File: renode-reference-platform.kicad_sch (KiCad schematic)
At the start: 4 parts

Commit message: [#95398] Cleanup
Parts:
- added H1, H2, H3, H4: Spacer_Drill3.7mm_H5mm_9774050151R, antmicro-footprints:Spacer_Drill3.7mm_H5mm_9774050151R, symbol antmicroMechanicalParts:Spacer_Drill3.7mm_H5mm_9774050151R
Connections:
- new net GND: H1.1, H2.1, H3.1, H4.1
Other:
- sheet IMU renamed Sensors
- sheet RPI Connector renamed Expansion Connector
- removed sheet PMOD
- sheet Expansion Connector: file rpi-expansion.kicad_sch -> expansion.kicad_sch
- sheet Expansion Connector ports: added none; removed EN_RPI_CONN, GPIO[0..27], I2C_RPI{I2C}, SPI_RPI{SPI}, UART_RPI{UART}
- sheet IOs ports: added POT1_Analog, POT2_Analog; removed none
- sheet MCU ports: added none; removed EN_PMOD, EN_RPI_CONN, GPIO[0..27], I2C3{I2C}, I2C4{I2C}, PMOD1_IO[5..8], PMOD2_IO[5..6], SPI_1{SPI}, SPI_2{SPI}, UART1{UART}, UART_3{UART}
- sheet Sensors: file imu.kicad_sch -> sensors.kicad_sch
- sheet Sensors ports: added I2C_SENSOR{I2C}; removed I2C_IMU{I2C}

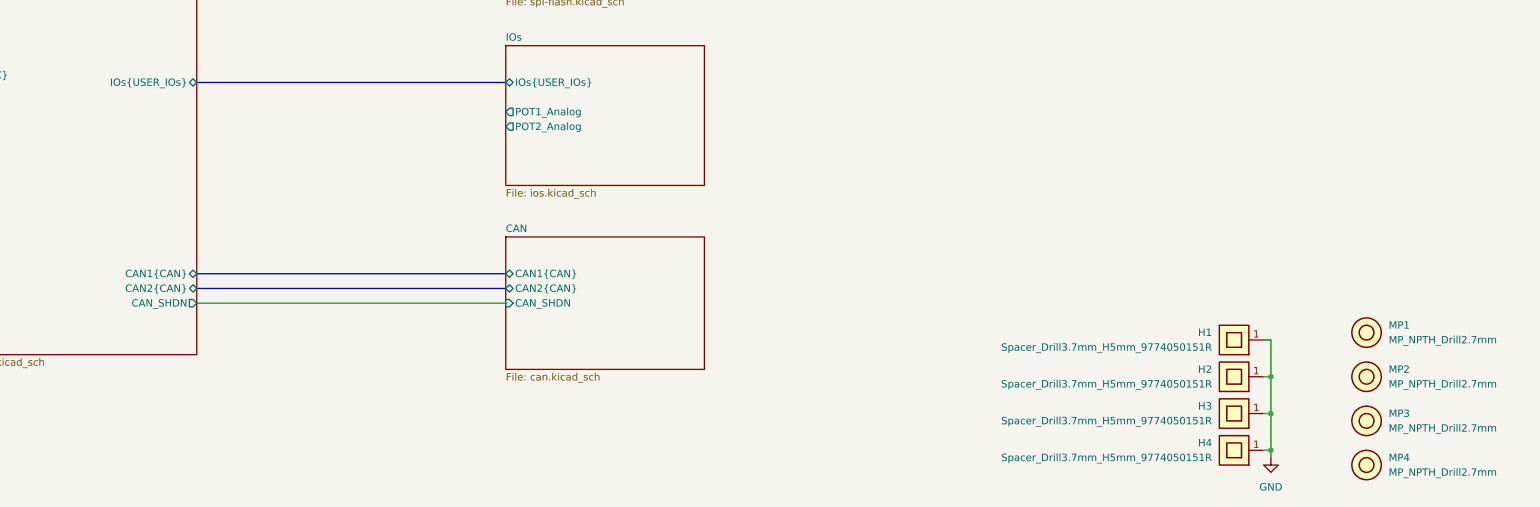
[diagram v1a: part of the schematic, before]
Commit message: [#95398] Connect potentiometers
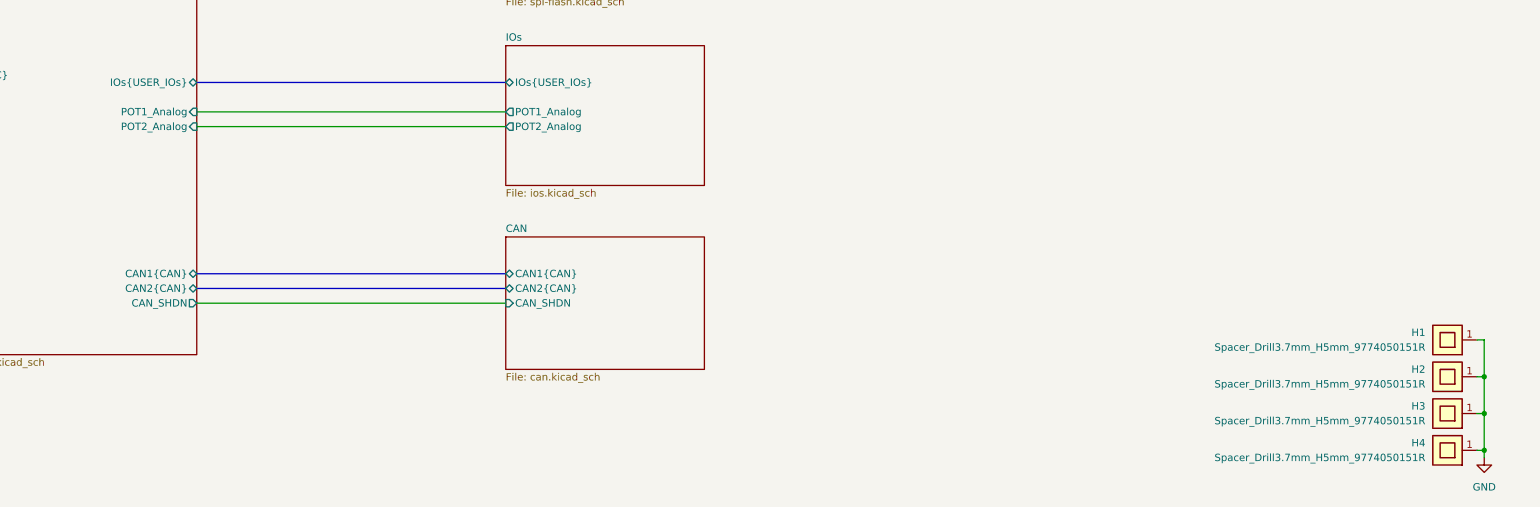
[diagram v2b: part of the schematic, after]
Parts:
- removed MP1, MP2, MP3, MP4: MP_NPTH_Drill2.7mm, antmicro-footprints:MP_NPTH_Drill2.7mm, symbol antmicroMechanicalParts:MP_NPTH_Drill2.7mm
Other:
- sheet MCU ports: added POT1_Analog, POT2_Analog; removed none
- moved on the sheet: H1, H2, H3, H4

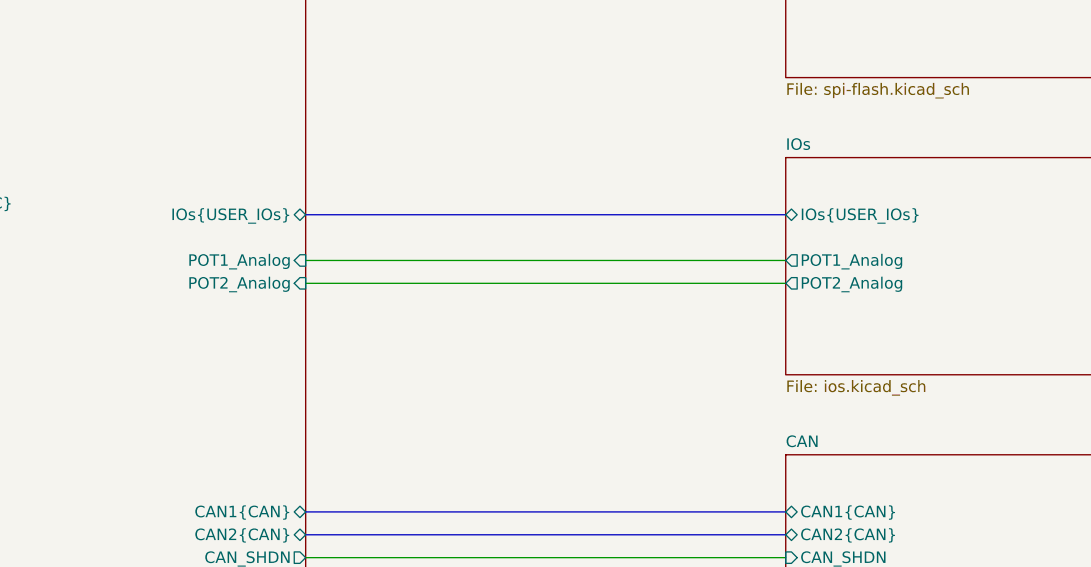
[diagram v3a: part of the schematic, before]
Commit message: [#95398] Mock main components, add BGA MCU
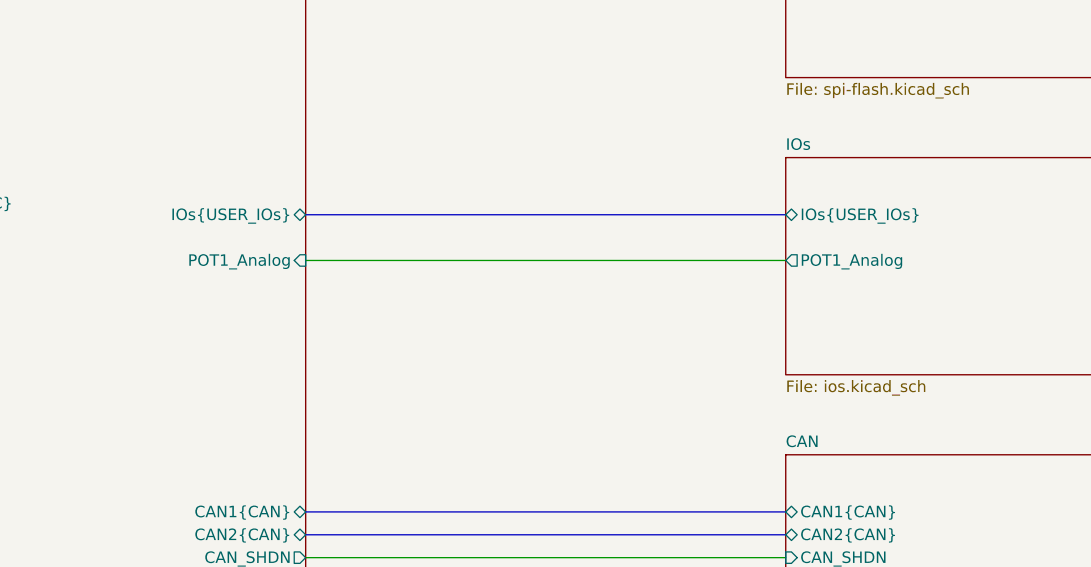
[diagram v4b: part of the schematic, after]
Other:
- sheet IOs ports: added none; removed POT2_Analog
- sheet MCU ports: added none; removed POT2_Analog
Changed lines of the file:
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@@
-	(wire
-		(pts
-			(xy 228.6 185.42) (xy 281.94 185.42)
-		)
-		(stroke
-			(width 0)
-			(type default)
-		)
-	)
 	(wire
 		(pts
@@
 			)
 		)
-		(pin "POT2_Analog" output
-			(at 281.94 185.42 180)
-			(effects
-				(font
-					(size 1.27 1.27)
-				)
-				(justify left)
-			)
-		)
 		(instances
 			(project "renode-reference-platform"
@@
 			(effects
 				(font
-					(size 1.27 1.27)
-				)
-				(justify right)
-			)
-		)
-		(pin "POT2_Analog" input
-			(at 228.6 185.42 0)
-			(effects
-				(font

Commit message: [#95398] Add markings for ETH strap resistors
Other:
- title: renode-reference-platform -> STM32H7 Renode Reference Platform
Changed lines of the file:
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@@
 	(paper "A3")
 	(title_block
-		(title "renode-reference-platform")
+		(title "STM32H7 Renode Reference Platform")
 		(date "07.04.2026")
 		(rev "1.0.0")

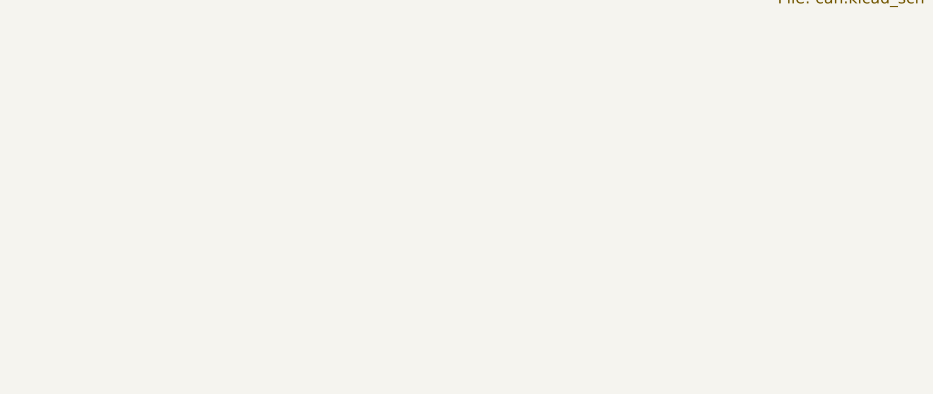
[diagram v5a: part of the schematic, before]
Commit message: [#95451] Fiducial and TP placement
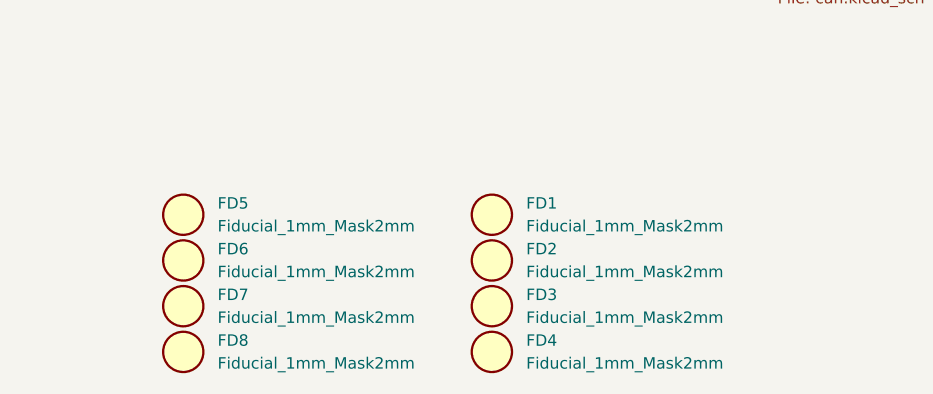
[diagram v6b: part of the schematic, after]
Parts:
- added FD1, FD2, FD3, FD4, FD5, FD6, FD7, FD8: Fiducial_1mm_Mask2mm, antmicro-footprints:Fiducial_1mm_Mask2mm, symbol antmicroFiducialMarks:Fiducial_1mm_Mask2mm

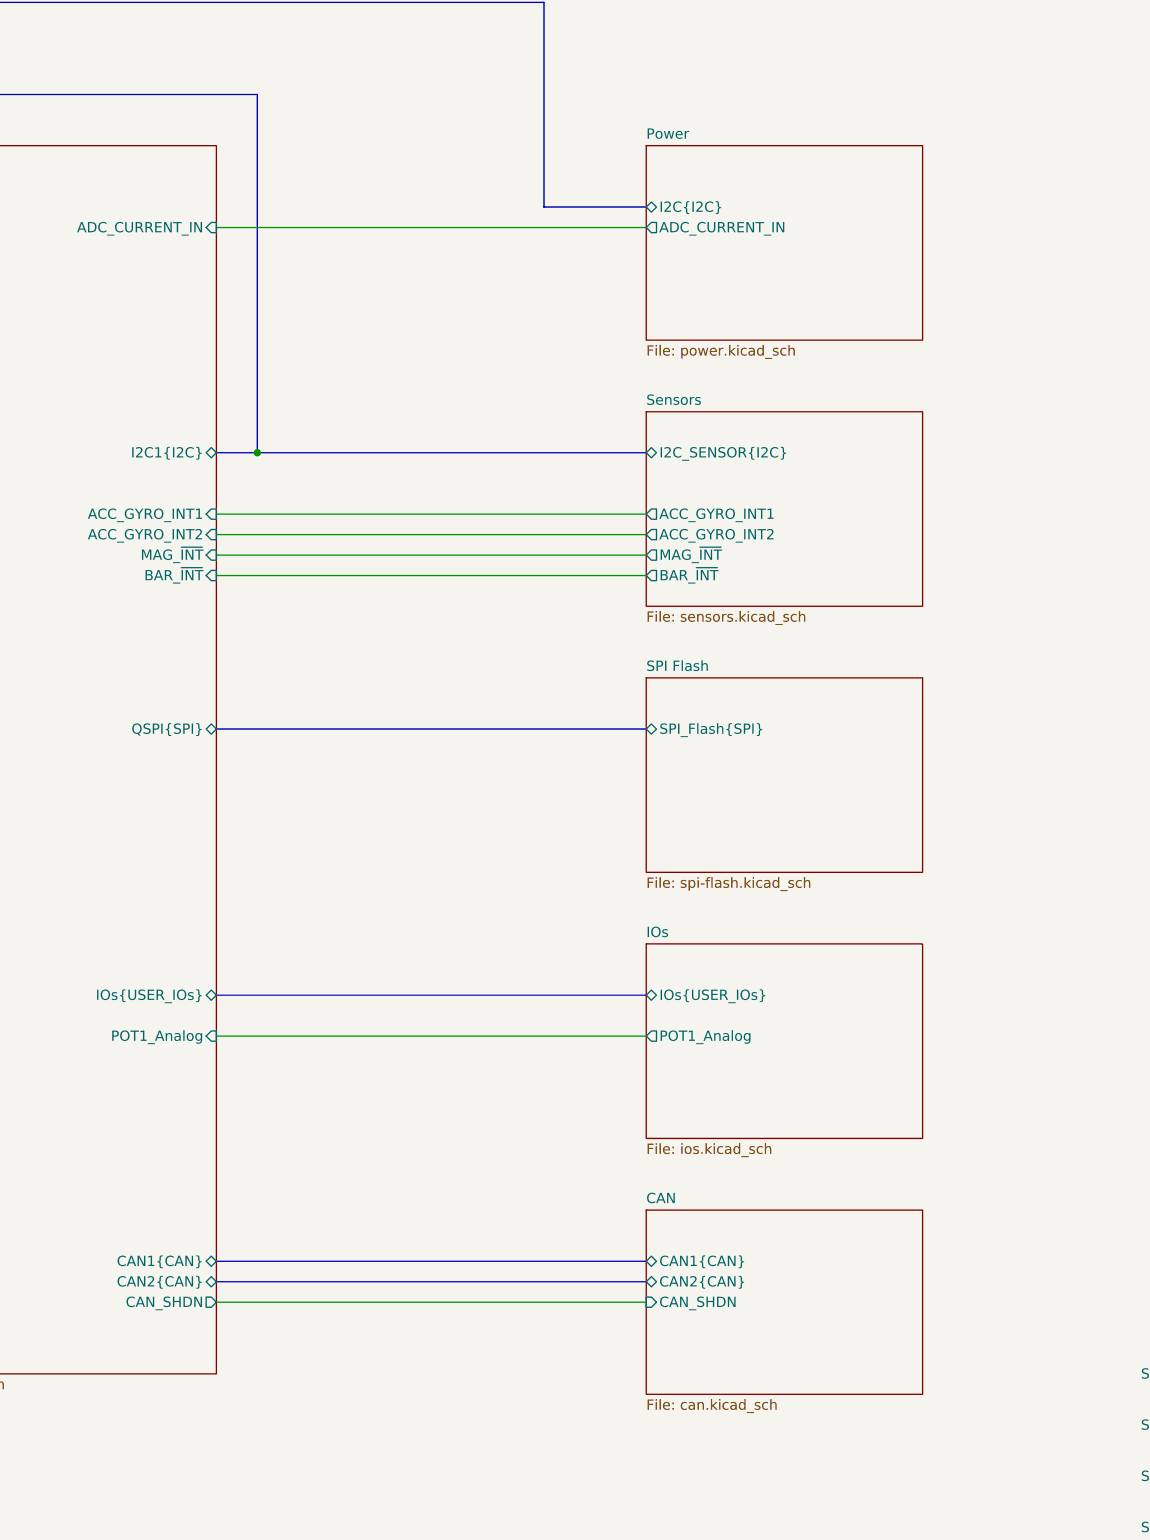
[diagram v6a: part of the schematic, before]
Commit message: [#95451] Improve placement. Add JTAG TC and ID EEPROM.
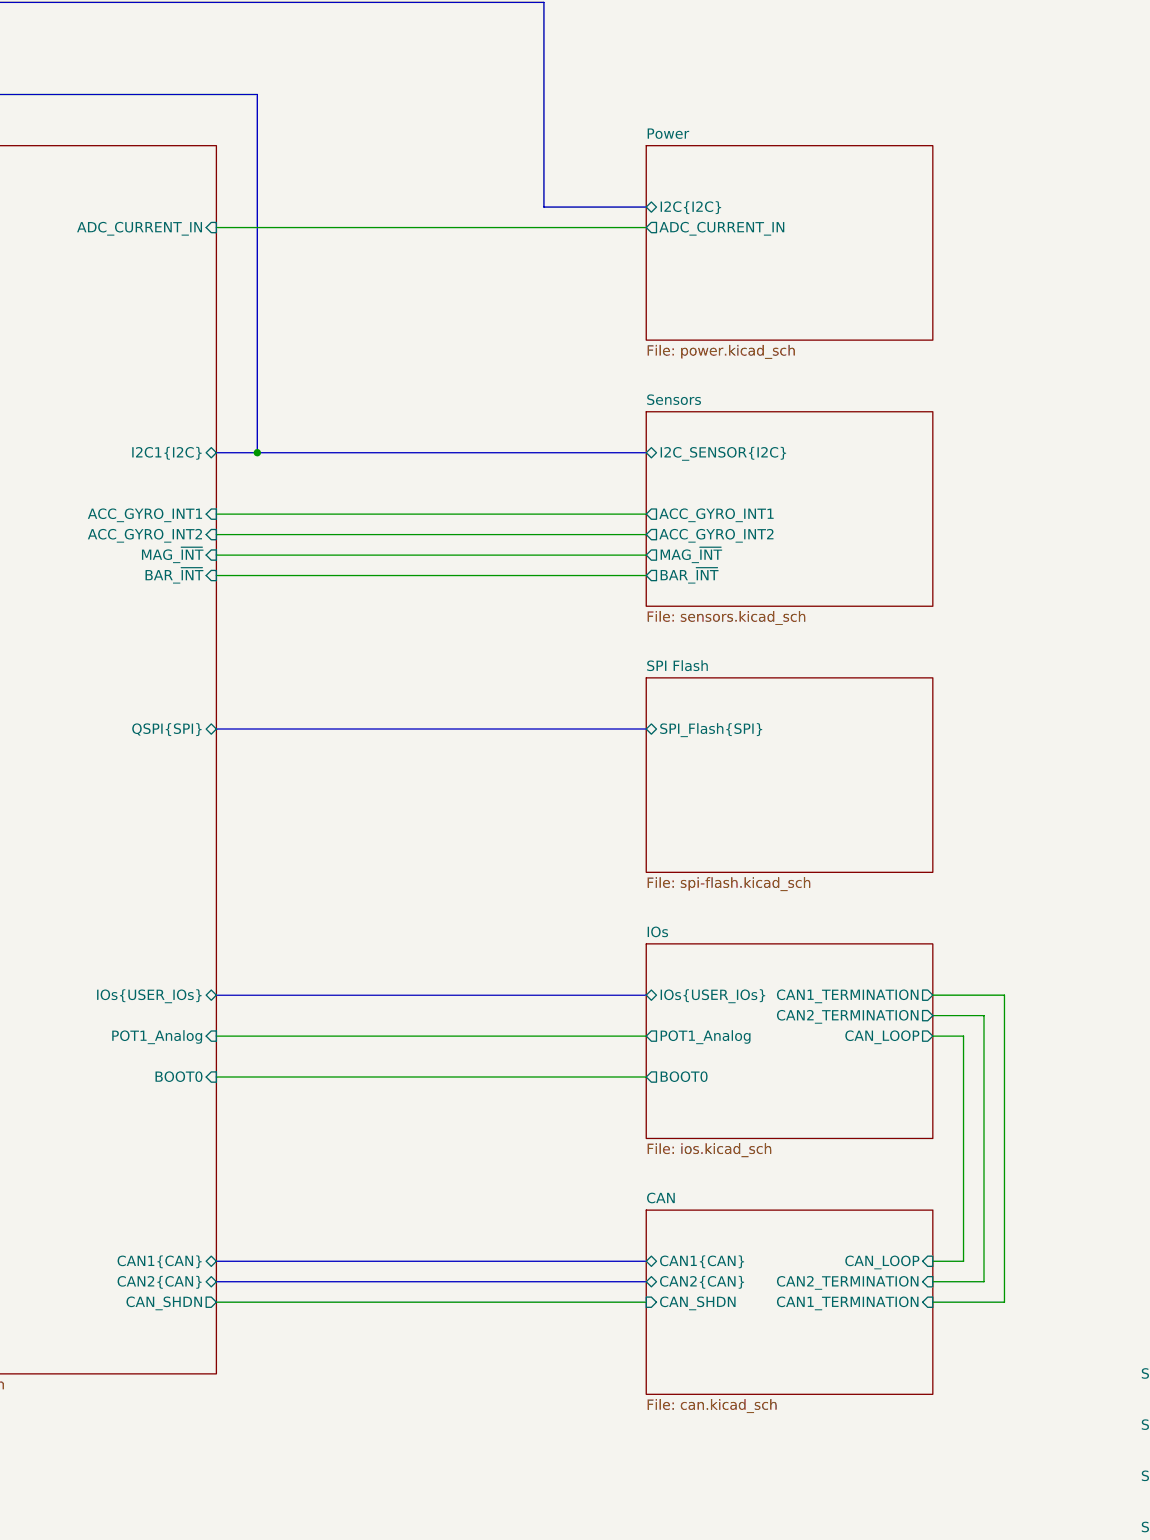
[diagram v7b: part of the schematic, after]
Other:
- sheet CAN ports: added CAN1_TERMINATION, CAN2_TERMINATION, CAN_LOOP; removed none
- sheet IOs ports: added BOOT0, CAN1_TERMINATION, CAN2_TERMINATION, CAN_LOOP; removed none
- sheet MCU ports: added BOOT0; removed none
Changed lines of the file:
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@@
+		)
+	)
+	(wire
+		(pts
+			(xy 317.5 180.34) (xy 323.85 180.34)
+		)
+		(stroke
+			(width 0)
+			(type default)
 		)
 	)
@@
 	(wire
 		(pts
+			(xy 321.31 210.82) (xy 317.5 210.82)
+		)
+		(stroke
+			(width 0)
+			(type default)
+		)
+	)
+	(wire
+		(pts
+			(xy 326.39 215.9) (xy 317.5 215.9)
+		)
+		(stroke
+			(width 0)
+			(type default)
+		)
+	)
+	(wire
+		(pts
 			(xy 228.6 82.55) (xy 281.94 82.55)
 		)
@@
 		)
 	)
+	(wire
+		(pts
+			(xy 321.31 182.88) (xy 321.31 210.82)
+		)
+		(stroke
+			(width 0)
+			(type default)
+		)
+	)
 	(bus
 		(pts
@@
 	(wire
 		(pts
+			(xy 323.85 213.36) (xy 317.5 213.36)
+		)
+		(stroke
+			(width 0)
+			(type default)
+		)
+	)
+	(wire
+		(pts
+			(xy 317.5 182.88) (xy 321.31 182.88)
+		)
+		(stroke
+			(width 0)
+			(type default)
+		)
+	)
+	(wire
+		(pts
 			(xy 388.62 223.52) (xy 389.89 223.52)
 		)
@@
 	(wire
 		(pts
+			(xy 323.85 180.34) (xy 323.85 213.36)
+		)
+		(stroke
+			(width 0)
+			(type default)
+		)
+	)
+	(wire
+		(pts
 			(xy 228.6 123.19) (xy 281.94 123.19)
 		)
@@
 		)
 	)
+	(wire
+		(pts
+			(xy 326.39 177.8) (xy 326.39 215.9)
+		)
+		(stroke
+			(width 0)
+			(type default)
+		)
+	)
 	(bus
 		(pts
@@
 	(wire
 		(pts
+			(xy 228.6 187.96) (xy 281.94 187.96)
+		)
+		(stroke
+			(width 0)
+			(type default)
+		)
+	)
+	(wire
+		(pts
 			(xy 129.54 123.19) (xy 185.42 123.19)
 		)
@@
 		(pts
 			(xy 388.62 242.57) (xy 389.89 242.57)
+		)
+		(stroke
+			(width 0)
+			(type default)
+		)
+	)
+	(wire
+		(pts
+			(xy 317.5 177.8) (xy 326.39 177.8)
 		)
 		(stroke
@@
 	(sheet
 		(at 281.94 105.41)
-		(size 34.29 24.13)
+		(size 35.56 24.13)
 		(exclude_from_sim no)
 		(in_bom yes)
@@
 	(sheet
 		(at 281.94 171.45)
-		(size 34.29 24.13)
+		(size 35.56 24.13)
 		(exclude_from_sim no)
 		(in_bom yes)
@@
 			)
 		)
+		(pin "BOOT0" output
+			(at 281.94 187.96 180)
+			(effects
+				(font
+					(size 1.27 1.27)
+				)
+				(justify left)
+			)
+		)
+		(pin "CAN1_TERMINATION" output
+			(at 317.5 177.8 0)
+			(effects
+				(font
+					(size 1.27 1.27)
+				)
+				(justify right)
+			)
+		)
+		(pin "CAN2_TERMINATION" output
+			(at 317.5 180.34 0)
+			(effects
+				(font
+					(size 1.27 1.27)
+				)
+				(justify right)
+			)
+		)
+		(pin "CAN_LOOP" output
+			(at 317.5 182.88 0)
+			(effects
+				(font
+					(size 1.27 1.27)
+				)
+				(justify right)
+			)
+		)
 		(instances
 			(project "renode-reference-platform"
@@
 	(sheet
 		(at 281.94 72.39)
-		(size 34.29 24.13)
+		(size 35.56 24.13)
 		(exclude_from_sim no)
 		(in_bom yes)
@@
 	(sheet
 		(at 281.94 204.47)
-		(size 34.29 22.86)
+		(size 35.56 22.86)
 		(exclude_from_sim no)
 		(in_bom yes)
@@
 				)
 				(justify left)
+			)
+		)
+		(pin "CAN1_TERMINATION" input
+			(at 317.5 215.9 0)
+			(effects
+				(font
+					(size 1.27 1.27)
+				)
+				(justify right)
+			)
+		)
+		(pin "CAN2_TERMINATION" input
+			(at 317.5 213.36 0)
+			(effects
+				(font
+					(size 1.27 1.27)
+				)
+				(justify right)
+			)
+		)
+		(pin "CAN_LOOP" input
+			(at 317.5 210.82 0)
+			(effects
+				(font
+					(size 1.27 1.27)
+				)
+				(justify right)
 			)
 		)
@@
 			)
 		)
+		(pin "BOOT0" input
+			(at 228.6 187.96 0)
+			(effects
+				(font
+					(size 1.27 1.27)
+				)
+				(justify right)
+			)
+		)
 		(instances
 			(project "renode-reference-platform"
@@
 	(sheet
 		(at 281.94 138.43)
-		(size 34.29 24.13)
+		(size 35.56 24.13)
 		(exclude_from_sim no)
 		(in_bom yes)
